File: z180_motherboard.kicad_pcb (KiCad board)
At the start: 2 copper layers, 1 part, among them U1 Z8S18033FSC

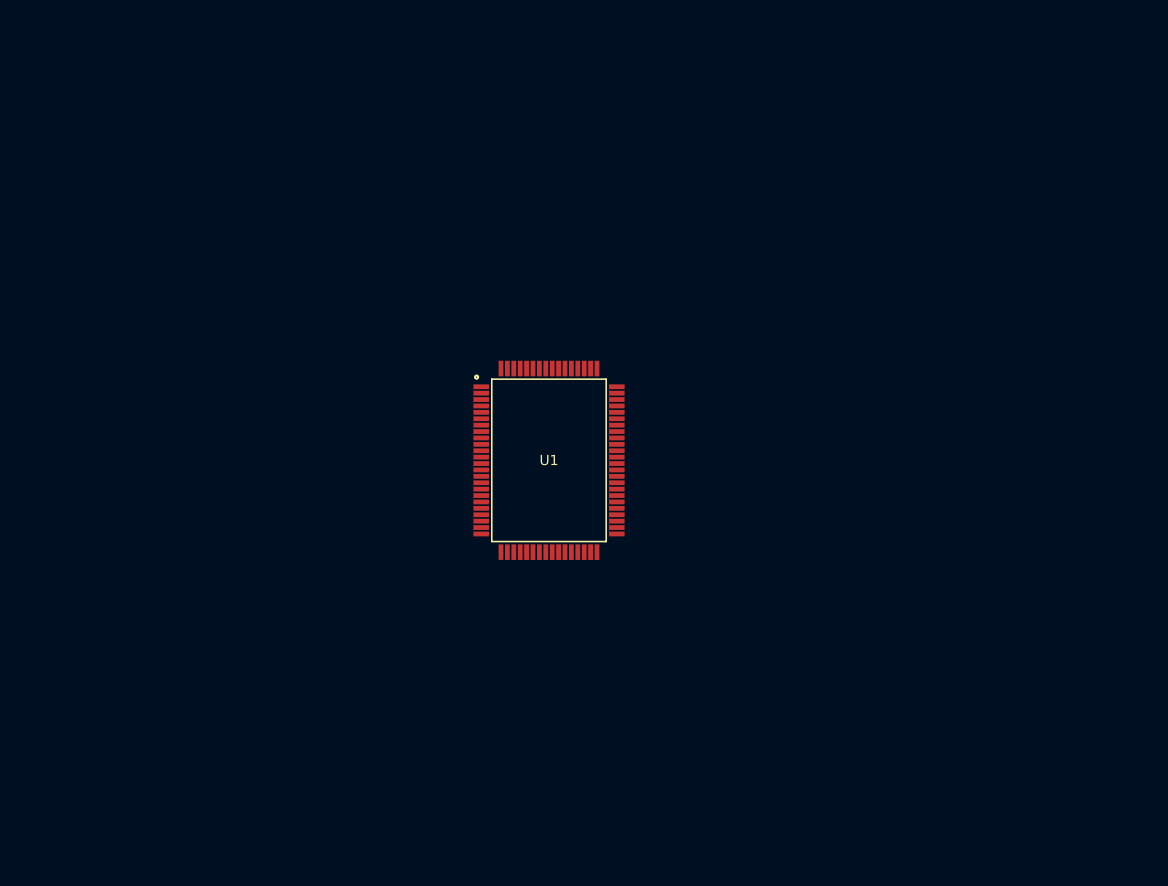
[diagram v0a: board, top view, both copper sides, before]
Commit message: added more chips
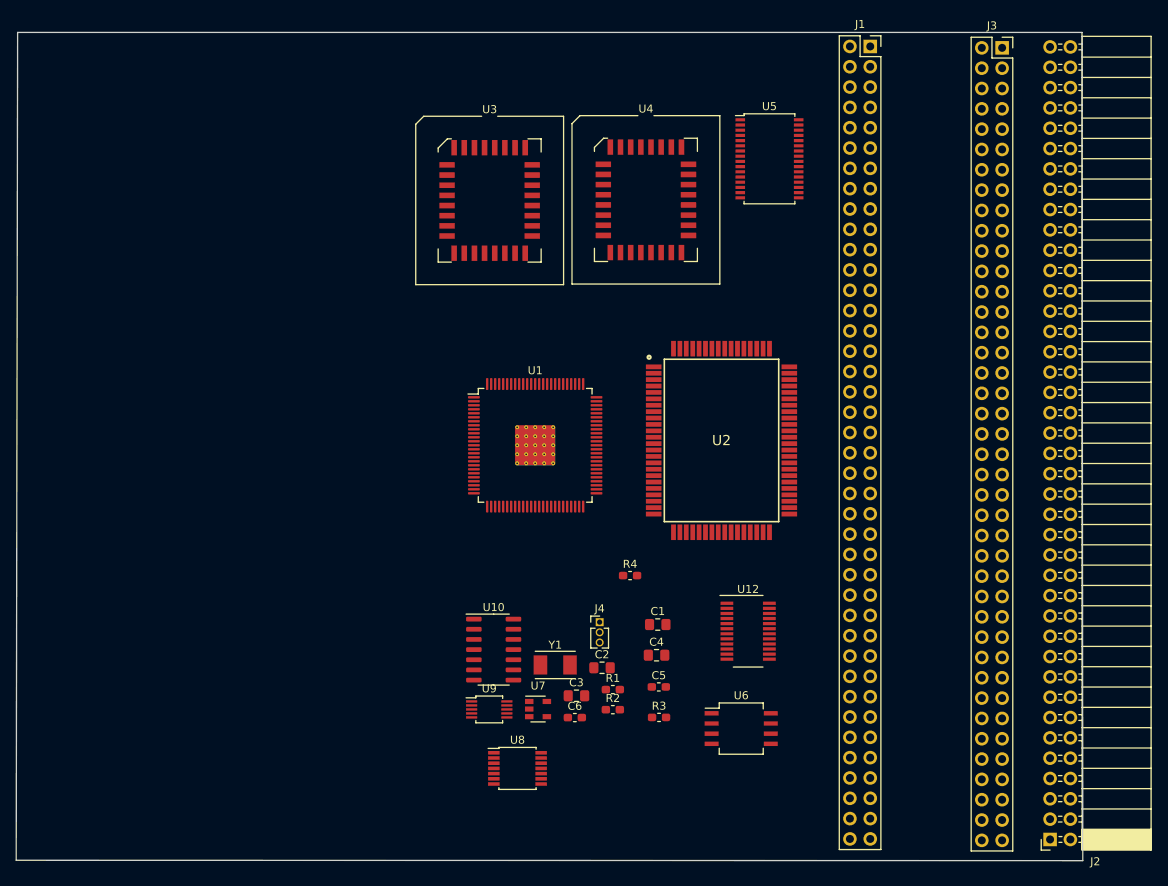
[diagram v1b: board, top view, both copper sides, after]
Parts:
- added C1: 22uF, Capacitor_SMD:C_0805_2012Metric_Pad1.15x1.40mm_HandSolder, F.Cu at (156.2, 112.3)
- added C2: 10uF, Capacitor_SMD:C_0805_2012Metric_Pad1.15x1.40mm_HandSolder, F.Cu at (149.2, 117.7)
- added C3: 100nF, Capacitor_SMD:C_0805_2012Metric_Pad1.15x1.40mm_HandSolder, F.Cu at (146.0, 121.2)
- added C4: 100nF, Capacitor_SMD:C_0805_2012Metric_Pad1.15x1.40mm_HandSolder, F.Cu at (156.0, 116.1)
- added C5: 0.47uF, Capacitor_SMD:C_0603_1608Metric_Pad1.05x0.95mm_HandSolder, F.Cu at (156.3, 120.1)
- added C6: 0.47uF, Capacitor_SMD:C_0603_1608Metric_Pad1.05x0.95mm_HandSolder, F.Cu at (145.8, 123.9)
- added J1: Conn_02x40_Counter_Clockwise, Connector_PinSocket_2.54mm:PinSocket_2x40_P2.54mm_Vertical, F.Cu at (182.8, 40.0)
- added J2: Conn_02x40_Counter_Clockwise, Connector_PinSocket_2.54mm:PinSocket_2x40_P2.54mm_Horizontal, F.Cu at (205.2, 139.1)
- added J3: Conn_02x40_Counter_Clockwise, Connector_PinSocket_2.54mm:PinSocket_2x40_P2.54mm_Vertical, F.Cu at (199.2, 40.2)
- added J4: UPDI TTL, Connector_PinHeader_1.27mm:PinHeader_1x03_P1.27mm_Vertical, F.Cu at (148.9, 112.0)
- added R1: 1K, Resistor_SMD:R_0603_1608Metric_Pad1.05x0.95mm_HandSolder, F.Cu at (150.6, 120.4)
- added R2: 1K, Resistor_SMD:R_0603_1608Metric_Pad1.05x0.95mm_HandSolder, F.Cu at (150.6, 122.9)
- added R3: 4K7, Resistor_SMD:R_0603_1608Metric_Pad1.05x0.95mm_HandSolder, F.Cu at (156.4, 123.9)
- added R4: 9.53K, Resistor_SMD:R_0603_1608Metric_Pad1.05x0.95mm_HandSolder, F.Cu at (152.7, 106.1)
- added U10: ATtiny1614-SS, Package_SO:SOIC-14_3.9x8.7mm_P1.27mm, F.Cu at (135.7, 115.4)
- added U12: AS1115-BSST, Package_SO:QSOP-24_3.9x8.7mm_P0.635mm, F.Cu at (167.5, 113.1)
- added U2: Z8S18033FSC, Package_QFP:QFP80P1792X2392X310-80N, F.Cu at (164.2, 89.3)
- added U3: SST39SF040, Package_LCC:PLCC-32_SMD-Socket, F.Cu at (135.2, 59.3)
- added U4: SST39SF040, Package_LCC:PLCC-32_SMD-Socket, F.Cu at (154.7, 59.2)
- added U5: AS6C4008-55PCN, Package_SO:TSSOP-32_6.1x11mm_P0.65mm, F.Cu at (170.2, 54.1)
- added U6: DS1302S+, Package_SO:SO-8_5.3x6.2mm_P1.27mm, F.Cu at (166.6, 125.3)
- added U7: TPS7A0533PDBVR, Package_TO_SOT_SMD:SOT-23-5, F.Cu at (141.2, 122.8)
- added U8: 74HC04, Package_SO:TSSOP-14_4.4x5mm_P0.65mm, F.Cu at (138.7, 130.3)
- added U9: Si5351A-B-GT, Package_SO:MSOP-10_3x3mm_P0.5mm, F.Cu at (135.1, 122.9)
- added Y1: 25MHZ 8PF, Crystal:Crystal_SMD_TXC_7A-2Pin_5x3.2mm, F.Cu at (143.4, 117.3)
- U1: value Z8S18033FSC -> EPM7064STC200; footprint Package_QFP:QFP80P1792X2392X310-80N -> Package_QFP:TQFP-100-1EP_14x14mm_P0.5mm_EP5x5mm_ThermalVias
- moved U1 2.55 mm to (140.9, 89.9)
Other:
- board outline added: 133.3 x 103.5 mm

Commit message: rewired to fit on 50mil grid
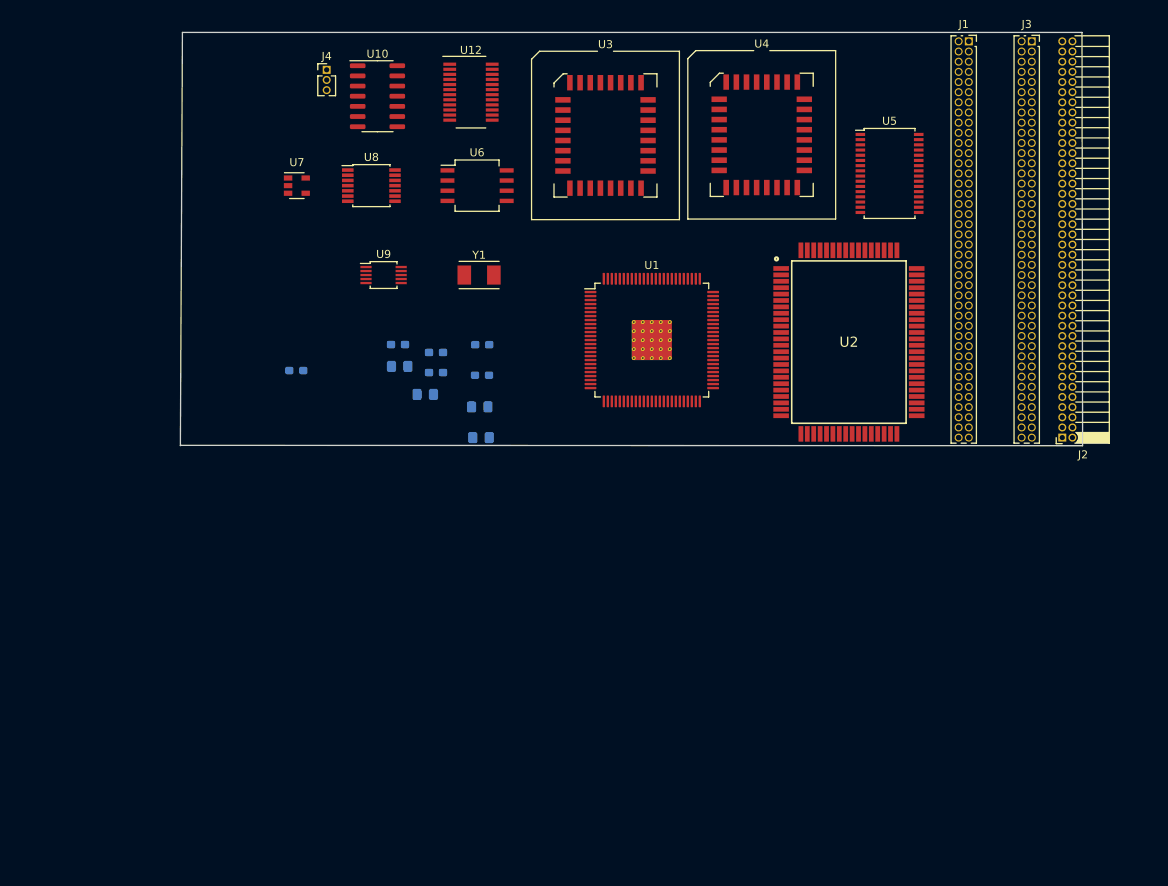
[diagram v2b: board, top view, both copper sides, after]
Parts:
- C1, C2, C3, C4, C5, C6, R1, R2, R3, R4: moved to B.Cu
- J1, J3: footprint Connector_PinSocket_2.54mm:PinSocket_2x40_P2.54mm_Vertical -> Connector_PinSocket_1.27mm:PinSocket_2x40_P1.27mm_Vertical
- J2: footprint Connector_PinSocket_2.54mm:PinSocket_2x40_P2.54mm_Horizontal -> Connector_PinSocket_1.27mm:PinSocket_2x40_P1.27mm_Horizontal
- moved J4 77.0 mm to (114.8, 42.9)
- moved U12 75.8 mm to (132.8, 45.7)
- moved U6 75.5 mm to (133.6, 57.4)
- moved U8 75.1 mm to (120.4, 57.4)
- moved U7 72.0 mm to (111.1, 57.4)
- moved U10 70.7 mm to (121.2, 46.2)
- moved U9 55.9 mm to (121.9, 68.6)
- moved C6 51.6 mm to (123.7, 77.3)
- moved R3 51.6 mm to (134.3, 77.3)
- moved J2 50.3 mm to (206.8, 88.9)
- moved R2 49.8 mm to (128.5, 78.3)
- moved Y1 49.7 mm to (133.9, 68.6)
- moved R4 49.0 mm to (111.0, 80.5)
- moved C3 46.7 mm to (123.9, 80.0)
- moved R1 45.4 mm to (128.5, 80.8)
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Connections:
- net /Sheet5D3BF5C8/IRQ renamed /IRQ
- net /Sheet5D3BF5C8/SCL renamed /SCL
- net /Sheet5D3BF5C8/SDA renamed /SDA
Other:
- board size 133.3 x 103.5 mm -> 112.8 x 51.7 mm
